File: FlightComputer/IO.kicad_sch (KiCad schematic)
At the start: 5 parts, among them J1 Conn_01x02_Pin, J2 USB C Plug (USB 2)

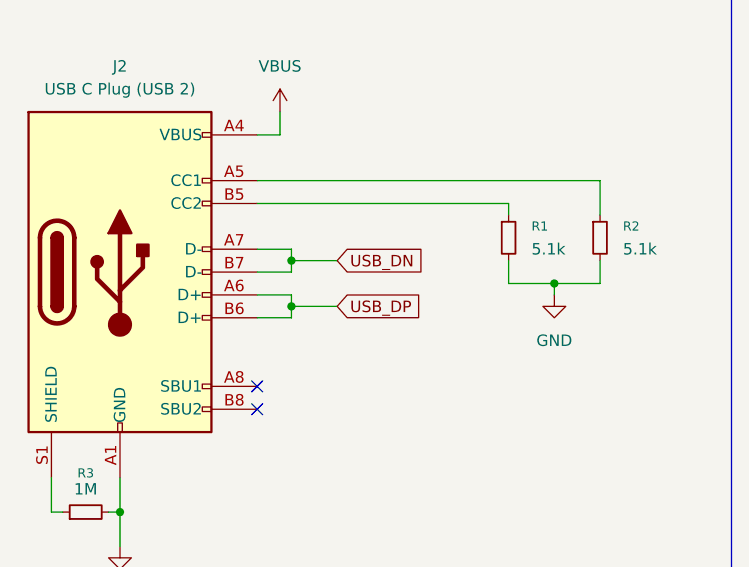
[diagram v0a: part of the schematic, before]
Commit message: Updating calculations, sensors page and adding micro page
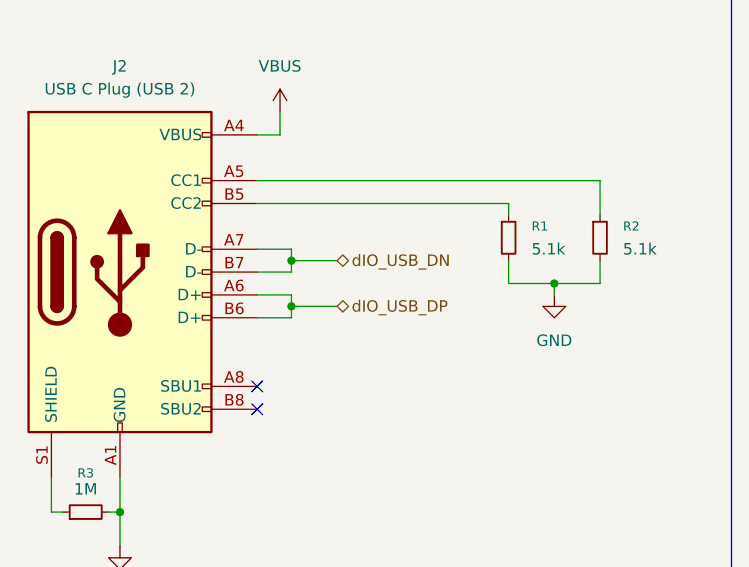
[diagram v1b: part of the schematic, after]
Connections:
- net USB_DN renamed dIO_USB_DN
- net USB_DP renamed dIO_USB_DP
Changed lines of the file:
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@@
 		)
 	)
-	(global_label "USB_DP"
-		(shape input)
+	(hierarchical_label "dIO_USB_DP"
+		(shape bidirectional)
 		(at 54.61 86.36 0)
-		(fields_autoplaced yes)
 		(effects
 			(font
@@
 			(justify left)
 		)
-		(property "Intersheetrefs" "${INTERSHEET_REFS}"
-			(at 64.9128 86.36 0)
-			(effects
-				(font
-					(size 1.27 1.27)
-				)
-				(justify left)
-				(hide yes)
-			)
-		)
 	)
-	(global_label "USB_DN"
-		(shape input)
+	(hierarchical_label "dIO_USB_DN"
+		(shape bidirectional)
 		(at 54.61 81.28 0)
-		(fields_autoplaced yes)
 		(effects
 			(font
@@
 			(justify left)
 		)
-		(property "Intersheetrefs" "${INTERSHEET_REFS}"
-			(at 64.9733 81.28 0)
-			(effects
-				(font
-					(size 1.27 1.27)
-				)
-				(justify left)
-				(hide yes)
-			)
-		)
 	)

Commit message: Various updates
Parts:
- added D5: RCLAMP0582B, Package_TO_SOT_SMD:SOT-416, symbol Power_Protection:RCLAMP0582B
- added H1, H2, H3, H4: MountingHole_Pad, MountingHole:MountingHole_3.2mm_M3_Pad, symbol Mechanical:MountingHole_Pad
- added J3: SWDIO/JTAG, symbol Connector_Generic:Conn_02x05_Odd_Even
- J2: footprint (none) -> Connector_USB:USB_C_Receptacle_GCT_USB4105-xx-A_16P_TopMnt_Horizontal
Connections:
- net GND: now also D5.3 (A), H1.1, H2.1, H3.1, H4.1, J3.3 (Pin_3), J3.5 (Pin_5), J3.7 (Pin_7), J3.9 (Pin_9)
- net dIO_USB_DN: now also D5.1 (K1)
- net dIO_USB_DP: now also D5.2 (K2)
- net USB_CC1: now reaches J2.A5 (CC1), R2.1
- net USB_CC2: now reaches J2.B5 (CC2), R1.1
- new net +3V3: J3.1 (Pin_1)
- new net JTAG_NRST: J3.10 (Pin_10)
- new net JTAG_TCK: J3.4 (Pin_4)
- new net JTAG_TDI: J3.8 (Pin_8)
- new net JTAG_TDO: J3.6 (Pin_6)
- new net JTAG_TMS: J3.2 (Pin_2)
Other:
- note added: "JTAG Programming Interface"
- company: (none) -> MD
- title: (none) -> Flight Computer: IO
- moved on the sheet: R1, R2
